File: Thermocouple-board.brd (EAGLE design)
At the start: 76.2 x 76.2 mm, 75 parts, among them J1 RJ45, J11 1X2-3.5MM, J12 1X2-3.5MM, J13 1X2-3.5MM, J14 1X2-3.5MM, J2 RJ45, J3 1981584-1, SW1 PUSHBUTTON, SW2 PUSHBUTTON, U1 STM32F042K4, U10 MAX31855, U11 MAX31855, U12 MAX31855, U13 MAX31855, U20 EEPROM-I2C, U21 EEPROM-I2C, U30 ST3485, U31 ST3485, U40 LP298XS, X1 NX3225GD

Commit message: WIP routing
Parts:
- moved SW2 74.1 mm to (71.6, 48.8), turned to 270 degrees
- moved C9 72.3 mm to (66.8, 51.3), flipped to the top, turned to 90 degrees
- moved R10 68.2 mm to (66.8, 46.7), flipped to the top, turned to 270 degrees
- moved SW1 65.8 mm to (71.6, 37.8), turned to 270 degrees
- moved C10 62.0 mm to (66.8, 40.4), flipped to the top, turned to 90 degrees
- moved R7 60.8 mm to (66.8, 35.8), flipped to the top, turned to 270 degrees
- moved R14 53.4 mm to (16.3, 36.8), turned to 90 degrees
- moved R15 43.1 mm to (24.4, 36.6), turned to 90 degrees
- moved C20 36.6 mm to (16.3, 32.5)
- moved U20 36.4 mm to (20.3, 32.5)
- moved C21 36.1 mm to (24.4, 32.5)
- moved U21 35.9 mm to (28.4, 32.5)
- moved D1 23.8 mm to (3.05, 26.7), turned to 180 degrees
- moved R11 23.2 mm to (2.79, 29.2)
- moved D2 21.4 mm to (2.79, 21.1), turned to 180 degrees
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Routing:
- net UART1_DE: track 1.32 -> 73.2 mm, vias 1 -> 4
- net UART1_RE_N: track 1.32 -> 67.4 mm, vias 1 -> 4
- net UART1_TX: track 1.32 -> 55.1 mm, vias 1 -> 4
- net SPI_CS1_N: track 9.37 -> 63.0 mm, vias 1 -> 4
- net SPI_MISO: track 51.1 -> 99.3 mm, vias 5 -> 7
- net SPI_SCK: track 40.5 -> 87.4 mm, vias 5 -> 7
- net SPI_CS0_N: track 8.81 -> 54.3 mm, vias 1 -> 4
- net I2C_SDA: track 58.1 -> 18.5 mm, vias 4 -> 2
- net I2C_SCL: track 57.1 -> 24.8 mm, vias 4 -> 0
- net GND: track 350.8 -> 371.0 mm
- net UART2_RE_N: track 1.32 -> 16.8 mm, vias 1 -> 2
- net USB_DP: track 21.9 -> 32.3 mm
- net USB_DM: track 21.4 -> 31.9 mm
- net UART2_DE: track 14.2 -> 23.7 mm, vias 1 -> 0
- net N$3: track 14.8 -> 5.76 mm
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
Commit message: WIP routing
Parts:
- moved C20 3.81 mm to (12.4, 32.5)
- moved R14 3.81 mm to (12.4, 36.8)
- moved C21 3.81 mm to (20.6, 32.5)
- moved R15 3.81 mm to (20.6, 36.6)
- moved U20 3.81 mm to (16.5, 32.5)
- moved U21 3.81 mm to (24.6, 32.5)
- moved C9 2.05 mm to (65.0, 50.3), turned to 180 degrees
- moved R10 1.85 mm to (65.0, 47.2), turned to 0 degrees
- moved C10 1.83 mm to (65.3, 39.4), turned to 180 degrees
- moved R7 1.61 mm to (65.3, 36.3), turned to 0 degrees
- moved R8 1.05 mm to (43.4, 27.9)
- moved SW1 1.02 mm to (70.6, 37.8)
- moved SW2 1.02 mm to (70.6, 48.8)
- moved JP1 0.57 mm to (71.6, 24.4)
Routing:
- net GND: track 371.0 -> 469.5 mm, vias 19 -> 22
- net SWDIO: track 0.00 -> 58.8 mm, vias 0 -> 1
- net NRST: track 0.00 -> 58.0 mm, vias 0 -> 2
- net SWCLK: track 0.00 -> 55.3 mm, vias 0 -> 1
- net LED_GRN: track 0.00 -> 41.4 mm, vias 0 -> 2
- net BTN_USER: track 0.05 -> 39.4 mm, vias 0 -> 2
- net LED_RED: track 0.00 -> 35.9 mm, vias 0 -> 2
- net UART1_RX: track 8.99 -> 43.5 mm, vias 1 -> 4
- net +3V3: track 290.6 -> 322.6 mm, vias 17 -> 18
- net UART1_RE_N: track 67.4 -> 42.3 mm
- net UART1_DE: track 73.2 -> 50.0 mm
- net UART1_TX: track 55.1 -> 38.8 mm
- net SPI_CS1_N: track 63.0 -> 56.7 mm
- net SPI_SCK: track 87.4 -> 81.4 mm
- net SPI_CS0_N: track 54.3 -> 49.1 mm
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
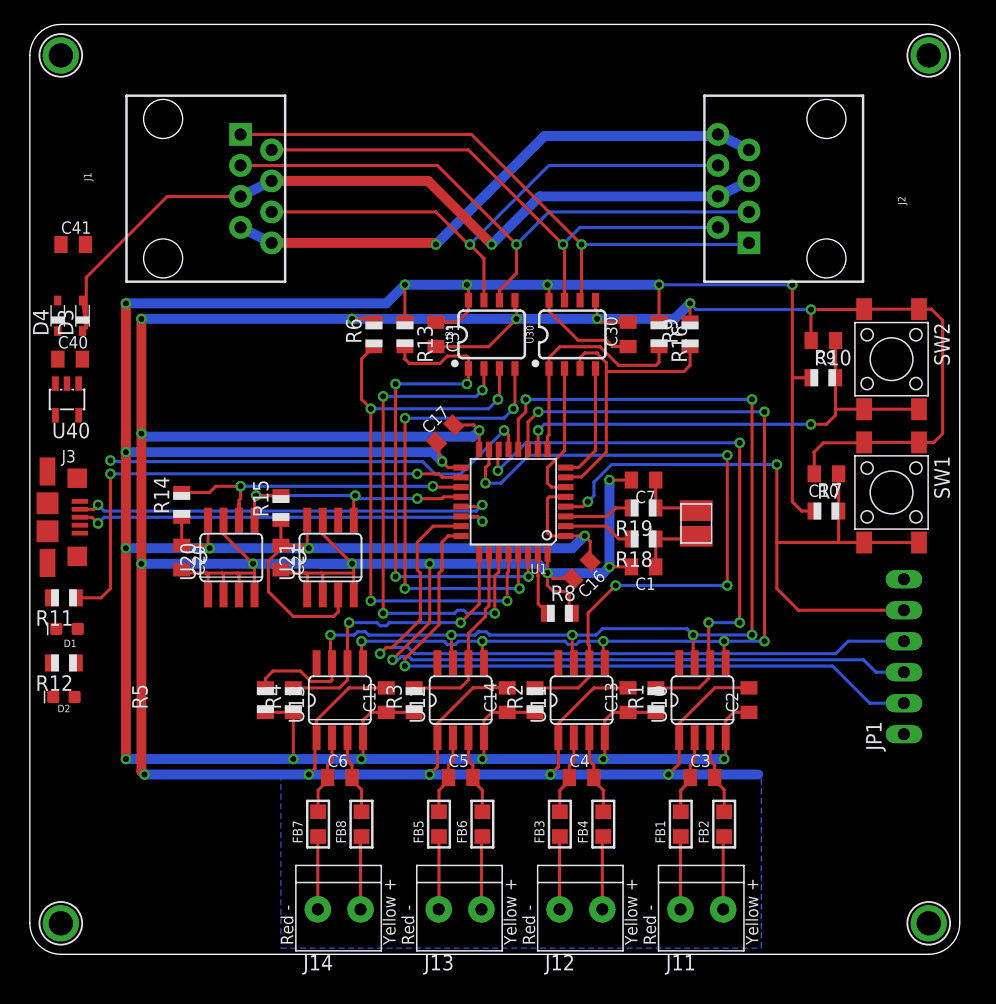
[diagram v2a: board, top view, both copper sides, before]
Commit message: Wip routing.  Updated DRC to Sparkfun and 20 mil vias with 10 mil annualar ring
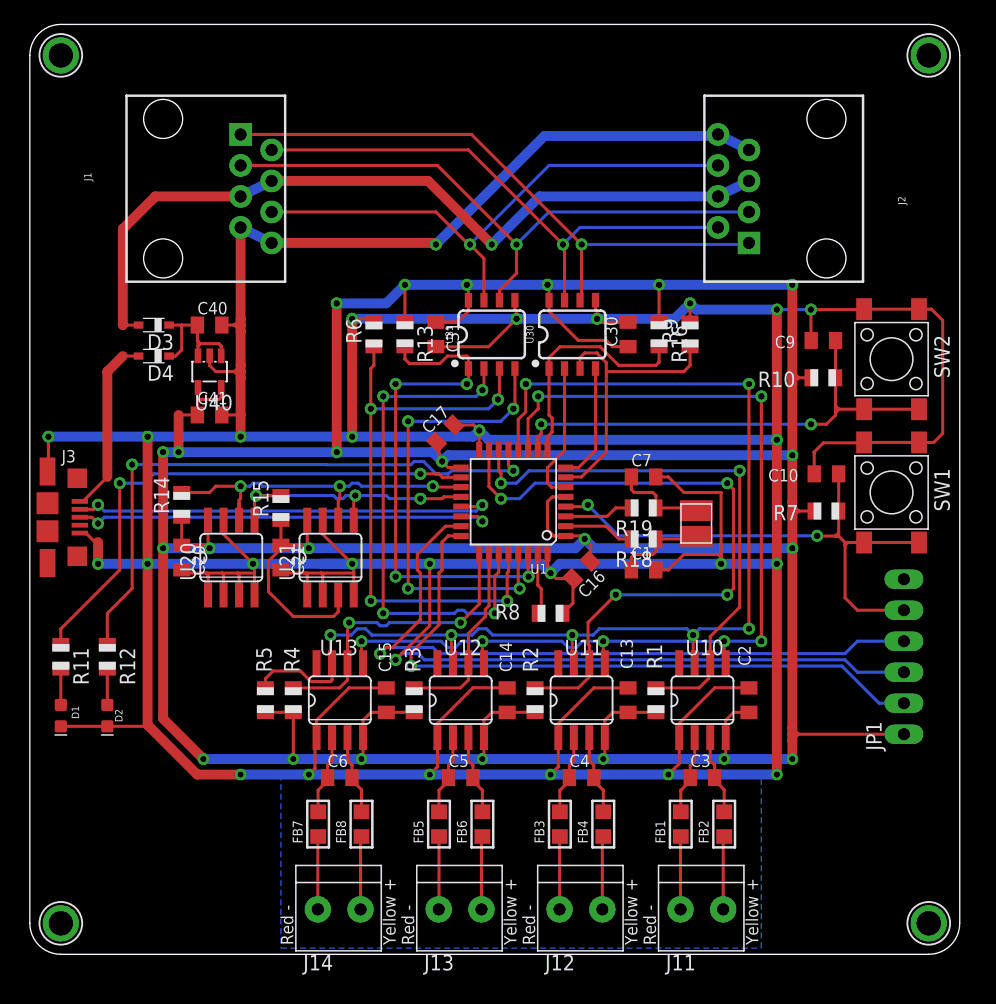
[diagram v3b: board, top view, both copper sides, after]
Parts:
- moved C41 17.9 mm to (14.7, 44.2)
- moved U40 11.9 mm to (14.7, 47.8)
- moved C40 11.8 mm to (14.7, 51.6)
- moved D4 8.54 mm to (10.2, 49.0), turned to 180 degrees
- moved D1 7.13 mm to (2.54, 19.6), turned to 270 degrees
- moved D3 5.89 mm to (10.2, 51.6), turned to 180 degrees
- moved R11 4.83 mm to (2.54, 24.4), turned to 270 degrees
- moved D2 3.87 mm to (6.35, 19.6), turned to 270 degrees
- moved R12 3.59 mm to (6.35, 24.4), turned to 270 degrees
- moved R8 0.76 mm to (42.7, 27.9)
- moved C1 0.25 mm to (50.3, 31.5), turned to 0 degrees
- moved C7 0.25 mm to (50.3, 39.1), turned to 0 degrees
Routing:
- net GND: track 469.5 -> 584.7 mm, vias 22 -> 28
- net +3V3: track 322.6 -> 389.5 mm, vias 18 -> 23
- net N$24: track 0.25 -> 14.8 mm
- net LED_RED: track 35.9 -> 49.4 mm
- net NRST: track 58.0 -> 45.9 mm
- net +5V: track 0.00 -> 11.3 mm
- net SPI_CS0_N: track 49.1 -> 45.7 mm, vias 4 -> 2
- net I2C_SCL: track 27.3 -> 30.6 mm, vias 2 -> 3
- net N$26: track 0.17 -> 2.95 mm
- net N$25: track 0.19 -> 2.95 mm
- net SPI_SCK: track 81.4 -> 83.9 mm
- net LED_GRN: track 41.4 -> 43.6 mm
- net SPI_MISO: track 95.3 -> 97.5 mm
- net SPI_CS1_N: track 56.7 -> 54.8 mm
- net N$19: track 5.70 -> 7.68 mm
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
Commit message: First pass routing commplete
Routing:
- net SWDIO: track 58.3 -> 59.4 mm
- net +3V3: track 389.5 -> 390.2 mm
- net UART1_RX: track 43.5 -> 44.0 mm

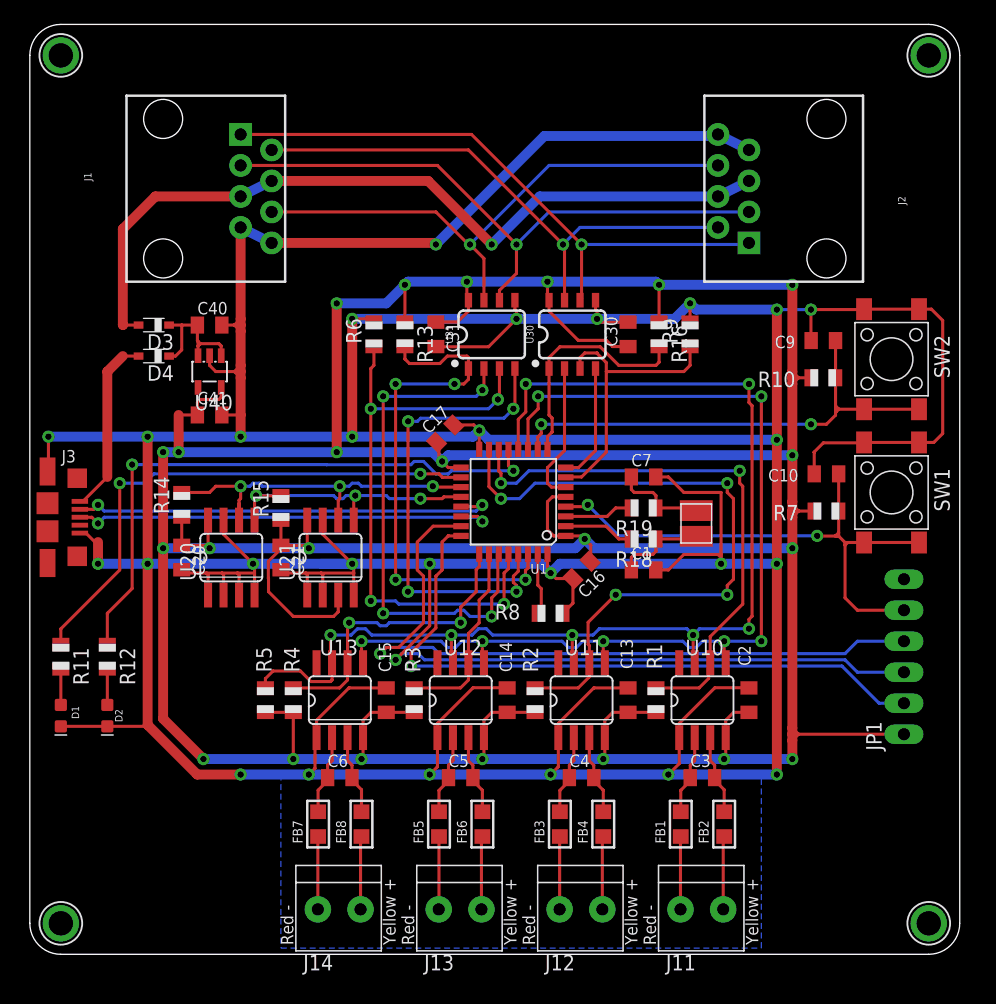
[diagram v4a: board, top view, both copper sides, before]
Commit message: Upgraded diodes; start of adding 5.5/2.5mm power connector
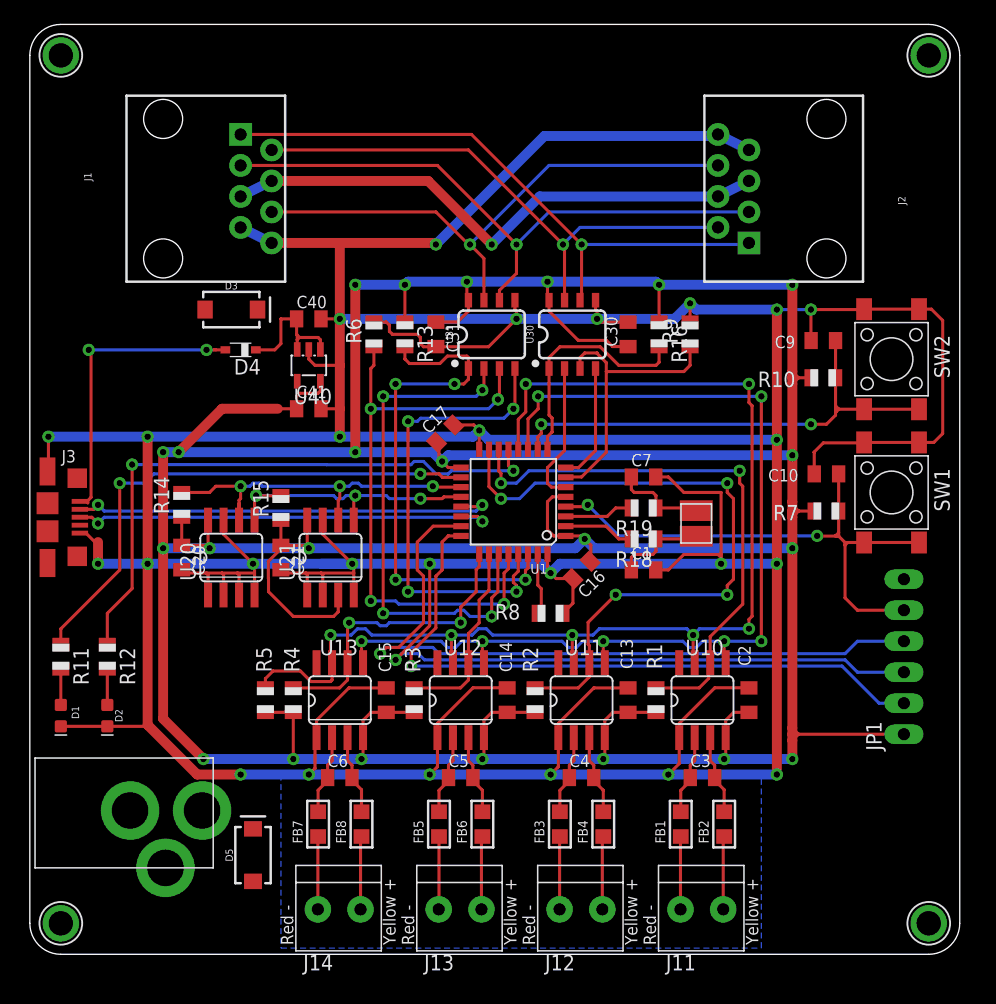
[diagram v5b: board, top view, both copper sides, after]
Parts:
- added D5: 3A/40V/500mV, SparkFun-DiscreteSemi:SMA-DIODE
- added J4: 2.1MMJACKTHM, adafruit:PJ-102A
- D3: value BAT60J -> 3A/40V/500mV; device diode:SOD323_ST -> SparkFun-DiscreteSemi:SMA-DIODE
- moved C40 8.14 mm to (22.9, 52.1)
- moved C41 8.14 mm to (22.9, 44.7)
- moved U40 8.14 mm to (22.9, 48.3)
- moved D4 7.13 mm to (17.3, 49.5)
- moved D3 6.48 mm to (16.5, 52.8), turned to 0 degrees
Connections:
- new net N$21: D5.A, J4.TIP
- net GND: now also J4.RING
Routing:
- net POE_PWR: track 66.0 -> 46.0 mm
- net N$24: track 14.8 -> 24.6 mm, vias 0 -> 2
- net GND: track 584.7 -> 576.6 mm, vias 28 -> 27
- net +3V3: track 390.2 -> 396.2 mm

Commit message: Routing complete
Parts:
- removed D4: BAT60J, diode:SOD323_ST
- removed D5: 3A/40V/500mV, SparkFun-DiscreteSemi:SMA-DIODE
- removed JP1: ST-LINK, Thermocouple-board:1X06_OVAL
- added C42: 10uF, adafruit:C0805K
- added J5: ST-LINK, Thermocouple-board:1X06_OVAL
- added J6: HEADER-1X3, Thermocouple-board:1X03_OVAL
- added J7: HEADER-1X2, Thermocouple-board:1X02_OVAL
- moved D2 3.59 mm to (5.84, 23.1)
- moved D1 3.57 mm to (2.29, 23.1)
- moved D3 3.53 mm to (18.3, 49.8), turned to 90 degrees
- moved R12 3.34 mm to (5.84, 27.7)
- moved R11 3.31 mm to (2.29, 27.7)
- moved J4 1.30 mm to (4.57, 10.4)
- moved C20 0.51 mm to (13.0, 32.5)
- moved R14 0.51 mm to (13.0, 36.8)
- moved C21 0.51 mm to (21.1, 32.5)
- moved R15 0.51 mm to (21.1, 36.6)
- moved U20 0.51 mm to (17.0, 32.5)
- moved U21 0.51 mm to (25.1, 32.5)
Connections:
- removed net N$21: D5.A, J4.TIP
- removed net N$24: D4.A, J3.1
- new net PWR: D3.A, J6.2, J7.1
- new net PWR_IN: J4.TIP, J6.1
- new net USB_VBUS: J3.1, J6.3
- net +3V3: now also C42.1, J5.1; no longer JP1.1
- net +5V: no longer D4.C
- net GND: now also C42.2, J5.3; no longer JP1.3
- net NRST: now also J5.5; no longer JP1.5
- net POE_PWR: now also J7.2; no longer D3.A
- net SWCLK: now also J5.2; no longer JP1.2
- net SWDIO: now also J5.4; no longer JP1.4
- net SWO: now also J5.6; no longer JP1.6
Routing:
- net PWR_IN: track 0.00 -> 41.7 mm
- net N$24: track 24.6 -> 0.00 mm, vias 2 -> 0
- net PWR: track 0.00 -> 19.9 mm
- net USB_VBUS: track 0.00 -> 13.6 mm
- net POE_PWR: track 46.0 -> 58.5 mm
- net GND: track 576.6 -> 588.0 mm, vias 27 -> 29
- net +3V3: track 396.2 -> 393.4 mm
- net +5V: track 11.3 -> 9.33 mm
- net SWDIO: track 59.4 -> 58.3 mm
- net SWCLK: track 54.6 -> 53.6 mm
- net NRST: track 45.9 -> 44.9 mm
- net LED_RED: track 49.4 -> 48.4 mm
- net I2C_SDA: track 23.3 -> 24.0 mm
